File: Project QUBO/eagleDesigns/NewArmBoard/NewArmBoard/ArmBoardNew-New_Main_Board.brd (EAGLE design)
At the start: 160 x 104 mm, 14 parts, among them U1 BME280

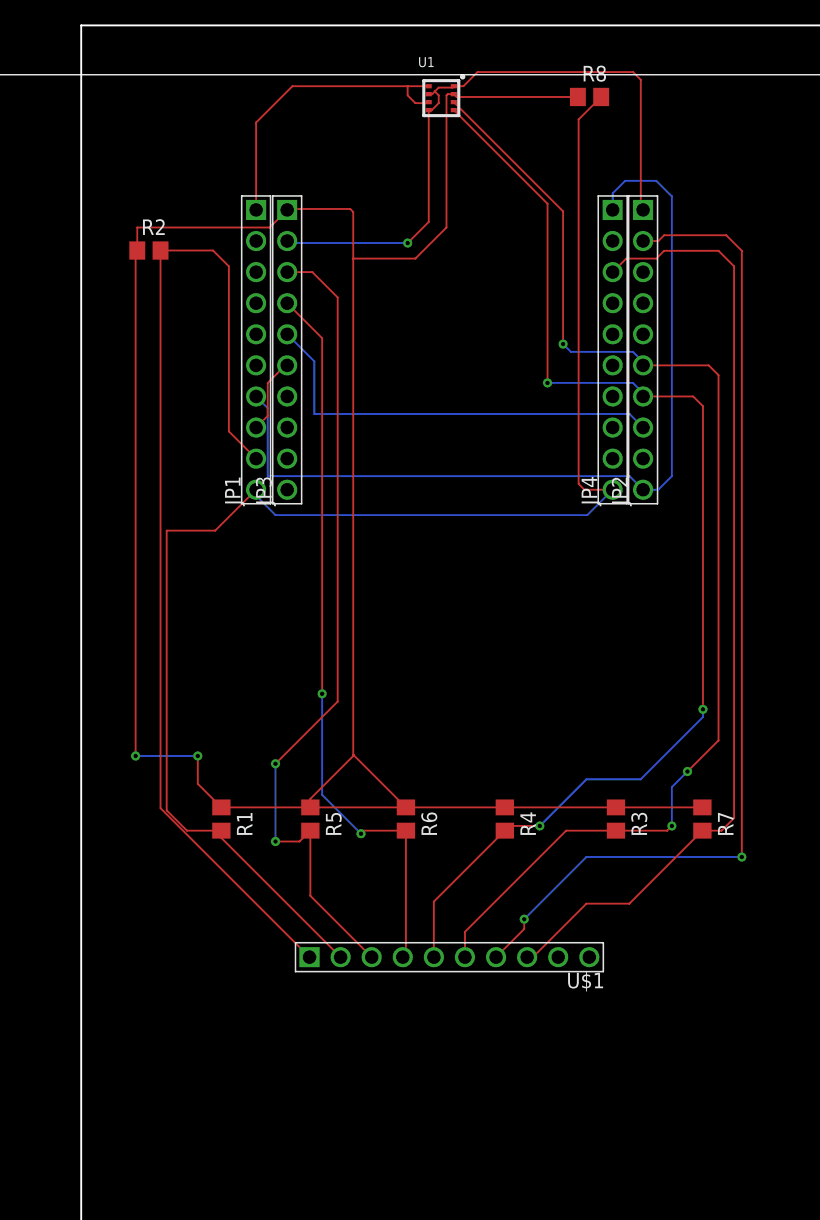
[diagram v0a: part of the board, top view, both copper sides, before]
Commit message: updated armboard schematic and brd layout
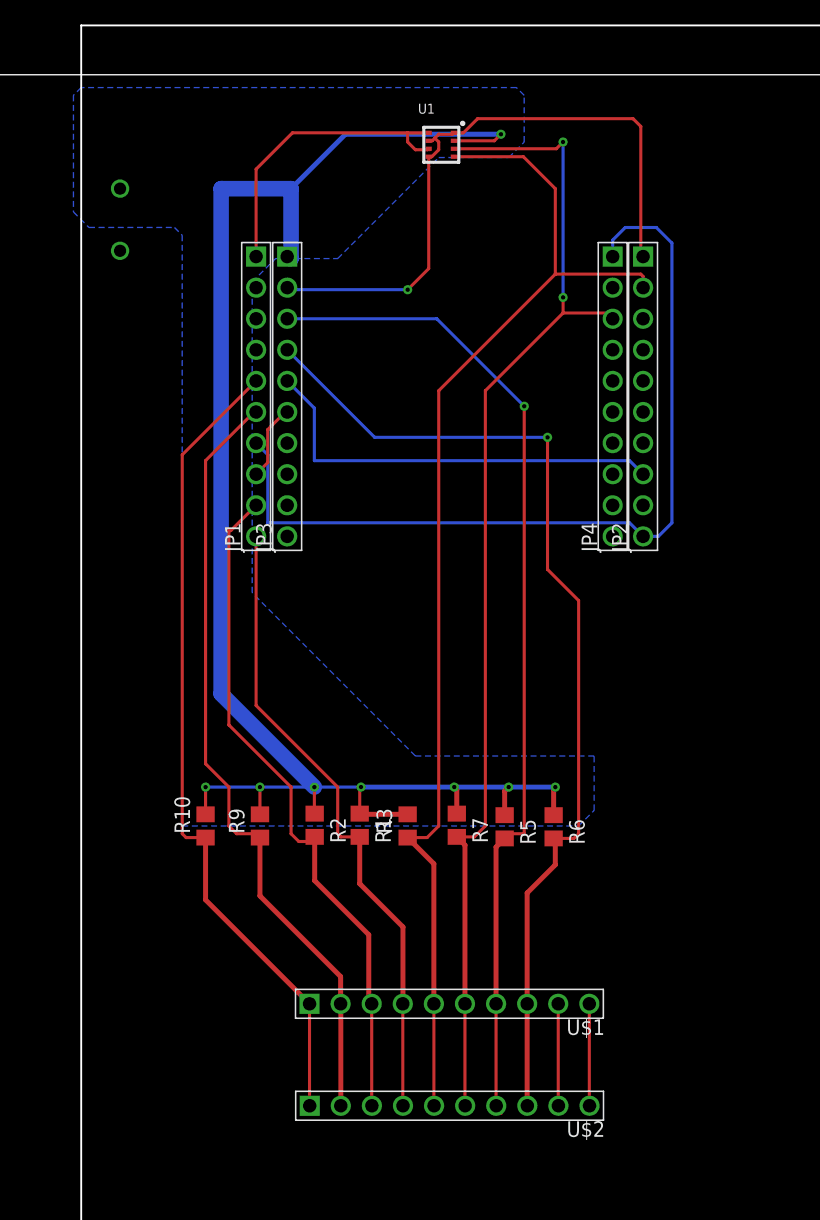
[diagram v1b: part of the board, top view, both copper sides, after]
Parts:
- removed R4, R8: 5k, resistor:R0805
- added R10, R9: 5k, resistor:R0805
- added U$2: KK254_10-PIN, molex:KK254_10-PIN
- moved R2 48.9 mm to (44.5, 36.3), turned to 270 degrees
- moved R7 20.1 mm to (56.1, 36.3)
- moved R3 17.0 mm to (52.1, 36.2), turned to 90 degrees
- moved R5 15.9 mm to (60.0, 36.1)
- moved R6 12.1 mm to (64.0, 36.1)
- moved R1 11.3 mm to (48.2, 36.3)
- moved JP1 3.81 mm to (39.7, 71.3)
- moved JP2 3.81 mm to (71.3, 71.3)
- moved JP3 3.81 mm to (42.2, 71.3)
- moved JP4 3.81 mm to (68.8, 71.3)
- moved U1 3.81 mm to (54.8, 91.8)
- moved U$1 3.81 mm to (55.5, 21.7)
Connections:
- removed net ACT_SCL: JP1.P$9, R2.2, U$1.P$1
- removed net ACT_SDA: JP1.P$10, JP4.P$10, R1.2, R8.2, U$1.P$2
- removed net BATT_SCL: JP3.P$3, R5.2, U$1.P$3
- removed net BATT_SDA: JP3.P$4, R6.2, U$1.P$4
- removed net EXT_SCL: JP2.P$7, R4.2, U$1.P$5, U1.P$4
- removed net EXT_SDA: JP2.P$6, R3.2, U$1.P$6, U1.P$3
- removed net INT_SCL: JP2.P$2, U$1.P$7
- removed net INT_SDA: JP4.P$3, R7.2, U$1.P$8
- removed net RX_PF: JP1.P$5
- removed net TX_PF: JP1.P$6
- new net MISO_2: JP2.P$7
- new net MOSI2: JP2.P$6
- new net PUSH1: JP4.P$10
- new net SCL_0: JP2.P$2, R3.1, U$1.P$5, U$2.P$5, U1.P$4
- new net SCL_1: JP1.P$9, R2.2, U$1.P$3, U$2.P$3
- new net SCL_2: JP1.P$5, R10.1, U$1.P$1, U$2.P$1
- new net SCL_3: JP3.P$3, R5.2, U$1.P$7, U$2.P$7
- new net SDA_0: JP4.P$3, R7.2, U$1.P$6, U$2.P$6, U1.P$3
- new net SDA_1: JP1.P$10, R1.2, U$1.P$4, U$2.P$4
- new net SDA_2: JP1.P$6, R9.1, U$1.P$2, U$2.P$2
- new net SDA_3: JP3.P$4, R6.2, U$1.P$8, U$2.P$8
- net 5V: now also R10.2, R3.2, R9.2; no longer R3.1, R4.1, R8.1
- net N$10: now also U$2.P$10
- net N$9: now also U$2.P$9
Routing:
- net ACT_SDA: track 117.6 -> 0.00 mm
- net SCL_0: track 0.00 -> 99.3 mm
- net EXT_SDA: track 98.4 -> 0.00 mm, vias 3 -> 0
- net SDA_0: track 0.00 -> 98.0 mm, vias 0 -> 2
- net EXT_SCL: track 97.3 -> 0.00 mm, vias 3 -> 0
- net ACT_SCL: track 85.5 -> 0.00 mm
- net SDA_3: track 0.00 -> 82.7 mm, vias 0 -> 1
- net INT_SCL: track 82.3 -> 0.00 mm, vias 2 -> 0
- net SCL_3: track 0.00 -> 82.2 mm, vias 0 -> 1
- net INT_SDA: track 77.9 -> 0.00 mm
- net SCL_2: track 0.00 -> 68.1 mm
- net BATT_SCL: track 67.2 -> 0.00 mm, vias 2 -> 0
- net SDA_2: track 0.00 -> 64.0 mm
- net 5V: track 197.6 -> 135.3 mm, vias 2 -> 9
- net BATT_SDA: track 60.1 -> 0.00 mm, vias 2 -> 0
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- added copper zone on layer 16, net 5V
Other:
- board text added: "ACT_SCL"

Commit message: created gerbers for arm board
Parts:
- moved R1 75.4 mm to (-4.55, -17.7)
- moved R10 75.4 mm to (-17.1, -17.8)
- moved R3 75.4 mm to (-0.64, -17.8)
- moved R5 75.4 mm to (7.29, -17.8)
- moved R6 75.4 mm to (11.3, -17.8)
- moved R7 75.4 mm to (3.38, -17.7)
- moved R9 75.4 mm to (-12.7, -17.8)
- moved U$1 75.4 mm to (2.78, -32.3)
- moved U$2 75.4 mm to (2.79, -40.6)
- moved U1 75.4 mm to (2.11, 37.9)
- moved JP1 75.4 mm to (-13.0, 17.3)
- moved JP2 75.4 mm to (18.6, 17.3)
- moved JP3 75.4 mm to (-10.5, 17.3)
- moved JP4 75.4 mm to (16.1, 17.3)
- moved R2 75.4 mm to (-8.23, -17.7)
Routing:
- net DGND: track 52.7 -> 67.6 mm
- net SCL_0: track 99.3 -> 109.3 mm, vias 0 -> 4
- net 5V: track 135.3 -> 144.2 mm
- net SDA_0: track 98.0 -> 101.9 mm, vias 2 -> 1
- net SPI_CLK: track 70.8 -> 72.2 mm, vias 1 -> 0
- added copper zone on layer 1, net DGND
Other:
- board size 160 x 104 mm -> 56.6 x 91.6 mm
- board text added: "5V-In"
- board text added: "ARM Shim Board Rev 1.0 Brendan Kane and Alex Jiao R@M 2018"
- board text added: "GND-In"
- board text added: "NC"
- board text added: "SCL_0"
- board text added: "SCL_1"
- board text added: "SCL_2"
- board text added: "SCL_3"
- board text added: "SDA_0"
- board text added: "SDA_1"
- board text added: "SDA_2"
- board text added: "SDA_3"
- board text removed: "ACT_SCL"
